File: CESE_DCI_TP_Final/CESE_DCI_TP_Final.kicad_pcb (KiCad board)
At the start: 2 copper layers, 100 x 100 mm, 55 parts, among them J1 Signal Inputs, J2 12V POWER, J3 POWER, M1 Motor 12V CC, Q1 IRFZ44NS, Q2 IRFZ44NS, Q3 IRFZ44NS, Q4 IRFZ44NS, Q5 BC337, Q6 BC337, U1 HIP4081A, U2 PC817, U3 PC817, U4 PC817, U5 ACS712, U6 LM358, U7 LM7805

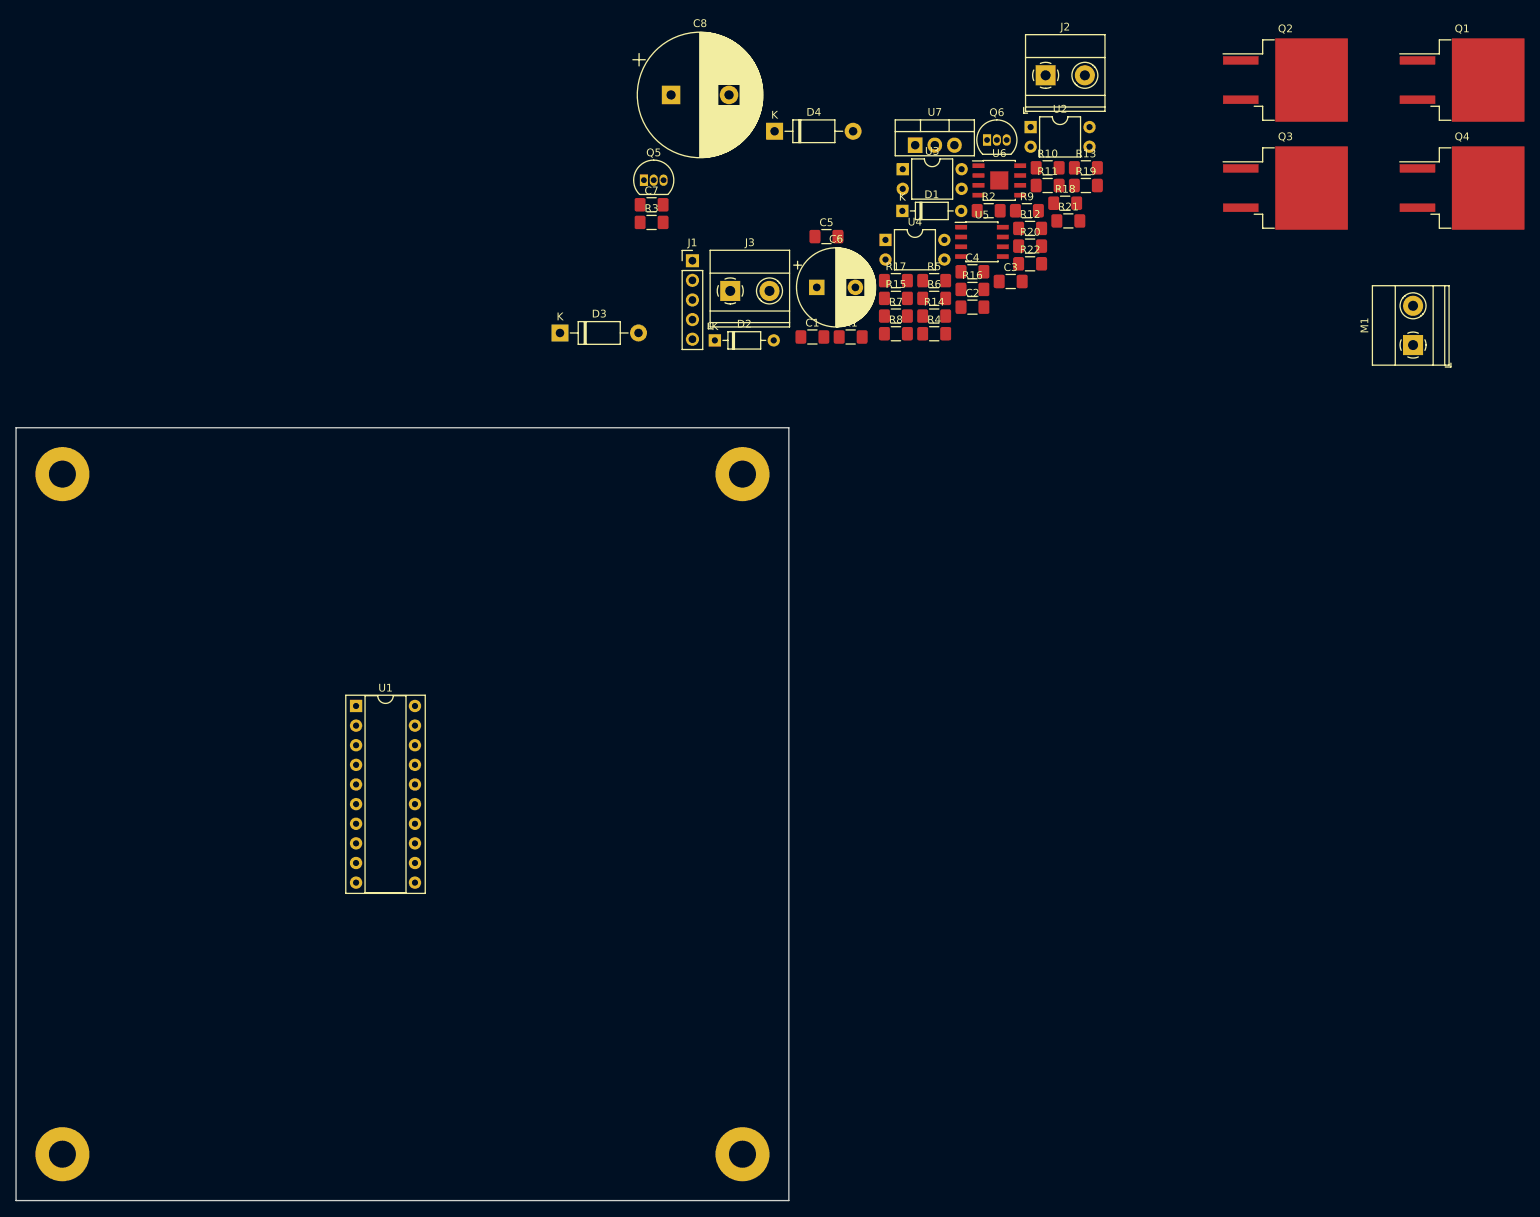
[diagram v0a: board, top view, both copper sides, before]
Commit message: Se finaliza PCB + 3D View + BOM
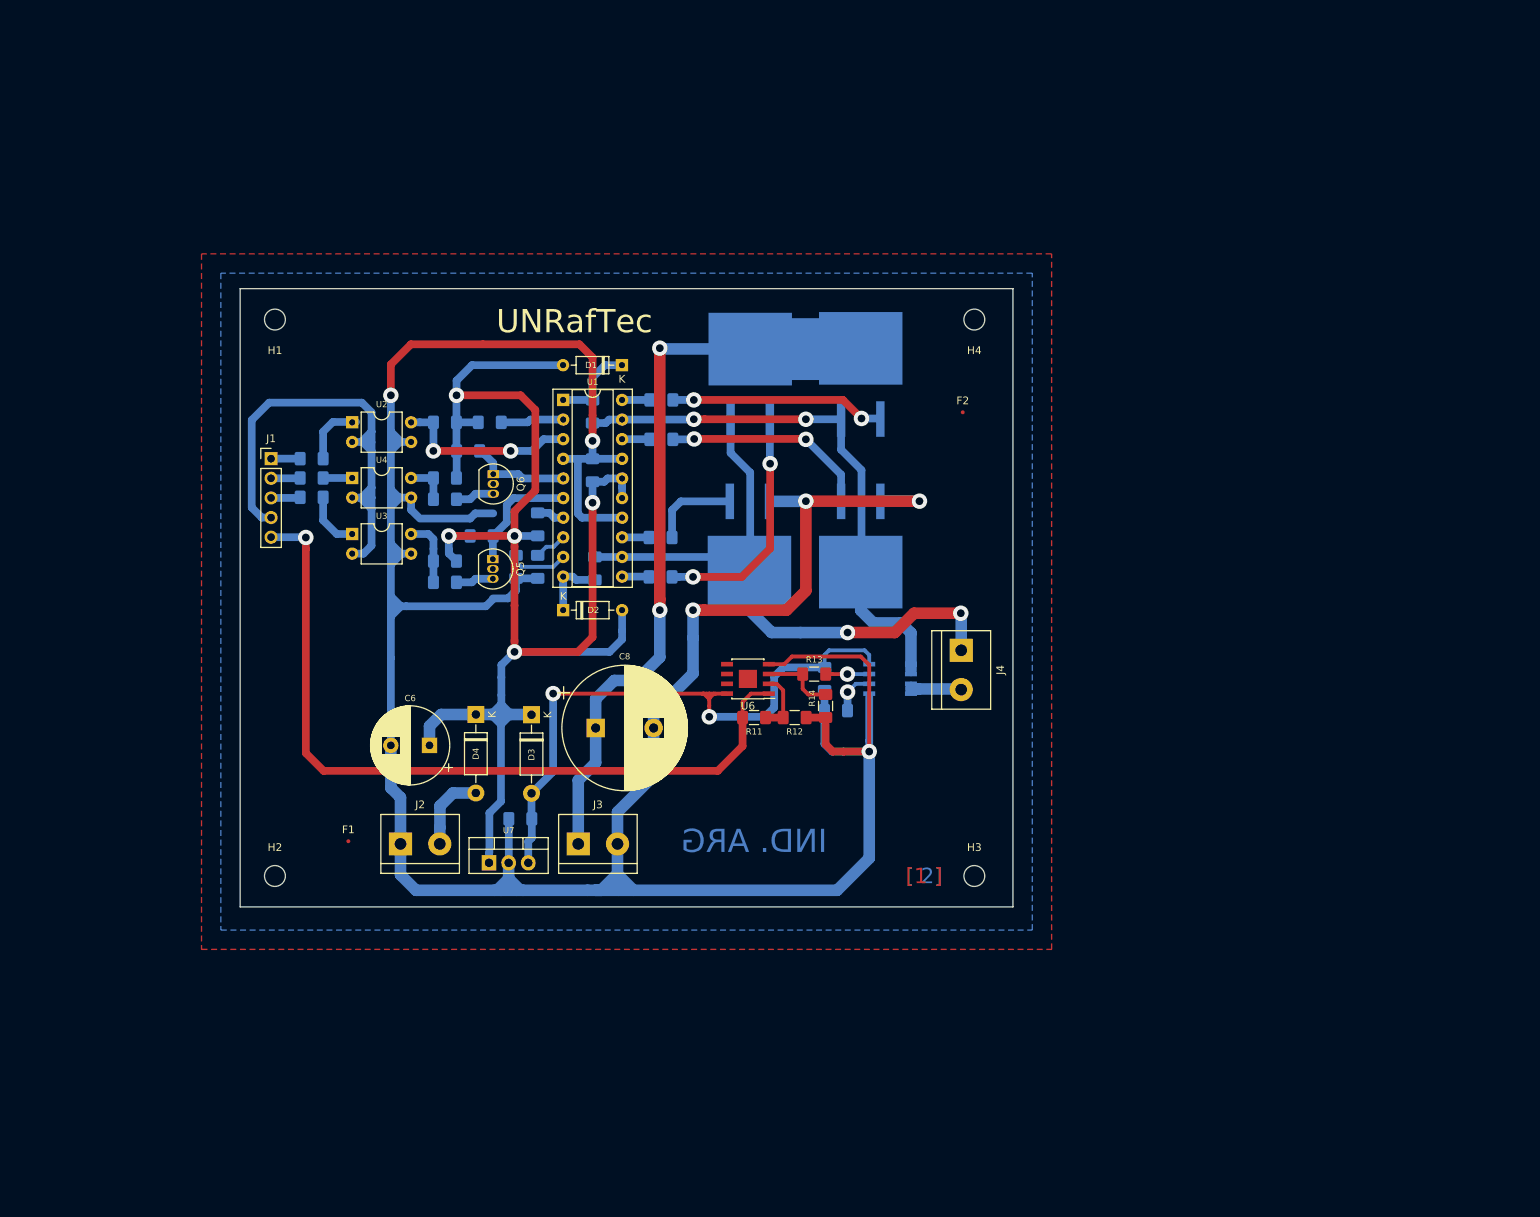
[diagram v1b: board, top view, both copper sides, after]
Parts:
- removed M1: Motor 12V CC, TerminalBlock_Phoenix:TerminalBlock_Phoenix_MKDS-1,5-2-5.08_1x02_P5.08mm_Horizontal
- removed REF** (x4): MountingHole_3.5mm_Pad, MountingHole:MountingHole_3.5mm_Pad
- added F1: Fiducial, Fiducial:Fiducial_0.5mm_Dia_1mm_Outer, F.Cu at (93.0, 123.5)
- added F2: Fiducial, Fiducial:Fiducial_0.5mm_Dia_1mm_Outer, F.Cu at (172.5, 68.0)
- added H1: MountingHole, MountingHole:MountingHole_2.7mm_M2.5, F.Cu at (83.5, 56.0)
- added H2: MountingHole, MountingHole:MountingHole_2.7mm_M2.5, F.Cu at (83.5, 128.0)
- added H3: MountingHole, MountingHole:MountingHole_2.7mm_M2.5, F.Cu at (174.0, 128.0)
- added H4: MountingHole, MountingHole:MountingHole_2.7mm_M2.5, F.Cu at (174.0, 56.0)
- added J4: Motor 12VCC, TerminalBlock:TerminalBlock_bornier-2_P5.08mm, F.Cu at (172.3, 98.8)
- C1, C2, C3, C4, C5, C7, Q1, Q2, Q3, Q4, R1, R10, R15, R16, R17, R18, R19, R2, R20, R21, R22, R3, R4, R5, R6, R7, R8, R9, U5: moved to B.Cu
- J2, J3: footprint TerminalBlock_Phoenix:TerminalBlock_Phoenix_MKDS-1,5-2-5.08_1x02_P5.08mm_Horizontal -> TerminalBlock:TerminalBlock_bornier-2_P5.08mm
- moved J2 129.8 mm to (99.8, 123.8)
- moved U7 108.0 mm to (111.2, 126.3)
- moved R19 107.1 mm to (88.2, 76.5)
- moved R10 102.4 mm to (88.2, 74.0), turned to 180 degrees
- moved U2 95.7 mm to (93.5, 69.3)
- moved Q4 95.3 mm to (145.0, 63.2), turned to 90 degrees
- moved R21 88.3 mm to (105.5, 79.2)
- moved R18 86.9 mm to (110.2, 84.0), turned to 180 degrees
- moved Q1 86.6 mm to (159.3, 63.1), turned to 90 degrees
- moved U3 85.5 mm to (93.5, 83.8)
- moved D4 84.8 mm to (109.5, 107.1), turned to 270 degrees
- moved Q3 83.4 mm to (144.9, 85.3), turned to 270 degrees
- moved C8 82.5 mm to (125.0, 108.8)
- moved Q2 81.6 mm to (159.3, 85.3), turned to 270 degrees
- moved R20 81.4 mm to (105.5, 76.5)
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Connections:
- net Net-(R9-Pad2) renamed /DIS
- C8 pad 2: GNDPWR -> GND
- J1 pad 2: /S-ALI -> /S-BLI
- J1 pad 3: /S-BLI -> /S-ALI
- J1 pad 4: /CURR -> GNDS
- J1 pad 5: GNDS -> /CURR
- J3 pad 2: GNDPWR -> GND
- Q2 pad 3: GNDPWR -> GND
- Q3 pad 3: GNDPWR -> GND
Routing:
- net GND: track 0.00 -> 431.5 mm, vias 0 -> 6
- net +12V: track 0.00 -> 199.1 mm, vias 0 -> 5
- net /CURR: track 0.00 -> 100.7 mm, vias 0 -> 1
- net VCC: track 0.00 -> 96.2 mm, vias 0 -> 2
- net /AHS: track 0.00 -> 80.3 mm, vias 0 -> 2
- net +5V: track 0.00 -> 79.7 mm, vias 0 -> 2
- net /BHS: track 0.00 -> 72.9 mm, vias 0 -> 2
- net GNDS: track 0.00 -> 64.4 mm
- net Net-(Q4-Pad1): track 0.00 -> 30.9 mm, vias 0 -> 2
- net Net-(Q1-Pad1): track 0.00 -> 27.9 mm, vias 0 -> 2
- net Net-(Q2-Pad1): track 0.00 -> 27.1 mm, vias 0 -> 2
- net /DIS: track 0.00 -> 24.0 mm, vias 0 -> 2
- net /ALI: track 0.00 -> 15.4 mm
- net /BLI: track 0.00 -> 13.3 mm
- net Net-(Q3-Pad1): track 0.00 -> 11.5 mm
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- added copper zone on B.Cu, net GND
- added copper zone on F.Cu, net GND
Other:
- board size 100 x 100 mm -> 100 x 80 mm
- net class Default: clearance 0.2 -> 0.25; trace_width 0.25 -> 0.5; via_dia 0.8 -> 2; via_drill 0.4 -> 1
- rule trace_clearance: 0.2 -> 0.25
- board text added: "Bungard CCD MTC: Grillas: 0,25mm, 0,2mm, 0,1mm Vía: 2mm / 1mm Márgen: 0,25mm Pistas: 0,5mm, 1mm, 1,5mm Dist. a borde: 0,3mm Terminación: HASL"
- board text added: "IND. ARG"
- board text added: "TP Final DCI"
- board text added: "UNRafTec"
- board text added: "[ 2]"
- board text added: "[1 ]"

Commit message: Se realizan correcciones
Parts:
- added F3: Fiducial, Fiducial:Fiducial_0.5mm_Dia_1mm_Outer, B.Cu at (154.9, 121.1)
- added F4: Fiducial, Fiducial:Fiducial_0.5mm_Dia_1mm_Outer, B.Cu at (77.7, 59.9)
- added G***: LOGO, CESE_DCI_TP_Final:logo_UNRaf, F.Cu at (162.8, 59.5)
- added G***: LOGO, CESE_DCI_TP_Final:logo_UNRaf, F.Cu at (154.2, 58.2)
- Q5, Q6: footprint Package_TO_SOT_THT:TO-92_Inline -> Package_TO_SOT_THT:TO-92_Inline_Wide
- U6: footprint Package_SO:SOIC-8-1EP_3.9x4.9mm_P1.27mm_EP2.35x2.35mm -> Package_SO:SOIC-8_3.9x4.9mm_P1.27mm
- moved C1 12.8 mm to (111.8, 75.5)
- moved C2 12.8 mm to (111.8, 67.9)
- moved C3 12.8 mm to (112.2, 88.2)
- moved C4 12.8 mm to (141.9, 102.5)
- moved C5 12.8 mm to (143.3, 106.6)
- moved C6 12.8 mm to (90.8, 111.1)
- moved C7 12.8 mm to (102.5, 120.6)
- moved C8 12.8 mm to (112.2, 108.8)
- moved D1 12.8 mm to (115.7, 61.9)
- moved D2 12.8 mm to (108.0, 93.6)
- moved D3 12.8 mm to (104.0, 107.1)
- moved D4 12.8 mm to (96.8, 107.1)
- moved F1 12.8 mm to (80.2, 123.5)
- moved F2 12.8 mm to (159.8, 68.0)
- moved H1 12.8 mm to (70.8, 56.0)
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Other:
- board text added: "Equipo de fabricación: Bungard CCD MTC Grillas utilizadas: 0,25mm, 0,2mm, 0,1mm Tamaño de vía: 2mm / 1mm Márgen utilizado: 0,25mm Ancho pistas: 0,5mm, 1mm, 1,5mm Dist. a borde: 0,3mm Terminación: HASL"
- board text added: "V1.0"
- board text removed: "Bungard CCD MTC: Grillas: 0,25mm, 0,2mm, 0,1mm Vía: 2mm / 1mm Márgen: 0,25mm Pistas: 0,5mm, 1mm, 1,5mm Dist. a borde: 0,3mm Terminación: HASL"
